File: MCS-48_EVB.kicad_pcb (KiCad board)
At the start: 2 copper layers, 36 parts, among them CON1 BARREL_JACK, P1 CONN_01X06, P10 CONN_01X08, P11 CONN_01X06, P2 CONN_01X06, P3 CONN_01X08, P4 CONN_01X08, P5 CONN_01X03, P6 CONN_01X03, P7 CONN_01X02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

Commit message: Working on component placement
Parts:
- C2, C4: moved to B.Cu
- moved U5 135.6 mm to (75.8, 97.2), turned to 180 degrees
- moved DS1 127.2 mm to (94.8, 52.9)
- moved U4 123.8 mm to (51.1, 97.2), turned to 180 degrees
- moved P3 109.5 mm to (52.1, 53.1), turned to 270 degrees
- moved U3 105.6 mm to (51.1, 139.8), turned to 180 degrees
- moved RV1 89.1 mm to (71.8, 59.8)
- moved P8 88.6 mm to (59.9, 104.3)
- moved U2 86.1 mm to (71.2, 139.8), turned to 180 degrees
- moved C2 78.7 mm to (69.9, 108.6), turned to 180 degrees
- moved C4 78.6 mm to (70.0, 103.7), turned to 180 degrees
- moved Y1 73.2 mm to (75.4, 108.6), turned to 90 degrees
- moved SW1 72.7 mm to (88.8, 146.5)
- moved P2 69.8 mm to (100.0, 155.2)
- moved CON1 68.8 mm to (196.2, 55.3), turned to 180 degrees
- moved C8 63.2 mm to (188.6, 56.2), turned to 90 degrees
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
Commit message: Finished component placement.
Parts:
- added C11: 100n, Capacitors_SMD:C_0805_HandSoldering, B.Cu at (38.9, 96.0)
- C1, C10, C3, C5, C6, C7, C9, R1, R2, R3: moved to B.Cu
- moved C5 101.7 mm to (67.4, 143.0), turned to 180 degrees
- moved C6 98.3 mm to (48.0, 138.4), turned to 90 degrees
- moved P3 96.1 mm to (59.0, 148.9)
- moved P6 94.9 mm to (77.0, 114.1), turned to 90 degrees
- moved C9 91.7 mm to (63.6, 95.9), turned to 90 degrees
- moved R3 84.9 mm to (61.3, 101.3), turned to 180 degrees
- moved P5 77.0 mm to (77.3, 149.0), turned to 90 degrees
- moved P2 65.9 mm to (153.0, 116.0), turned to 180 degrees
- moved C8 58.7 mm to (145.0, 95.5)
- moved P7 57.3 mm to (137.5, 145.2)
- moved CON1 57.2 mm to (154.6, 94.7)
- moved R1 54.4 mm to (90.6, 101.5)
- moved C1 51.6 mm to (98.5, 128.3), turned to 90 degrees
- moved C7 48.9 mm to (90.5, 99.2)
- moved R2 47.2 mm to (125.7, 147.7)
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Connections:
- U4 pad 28: VCC -> +5V

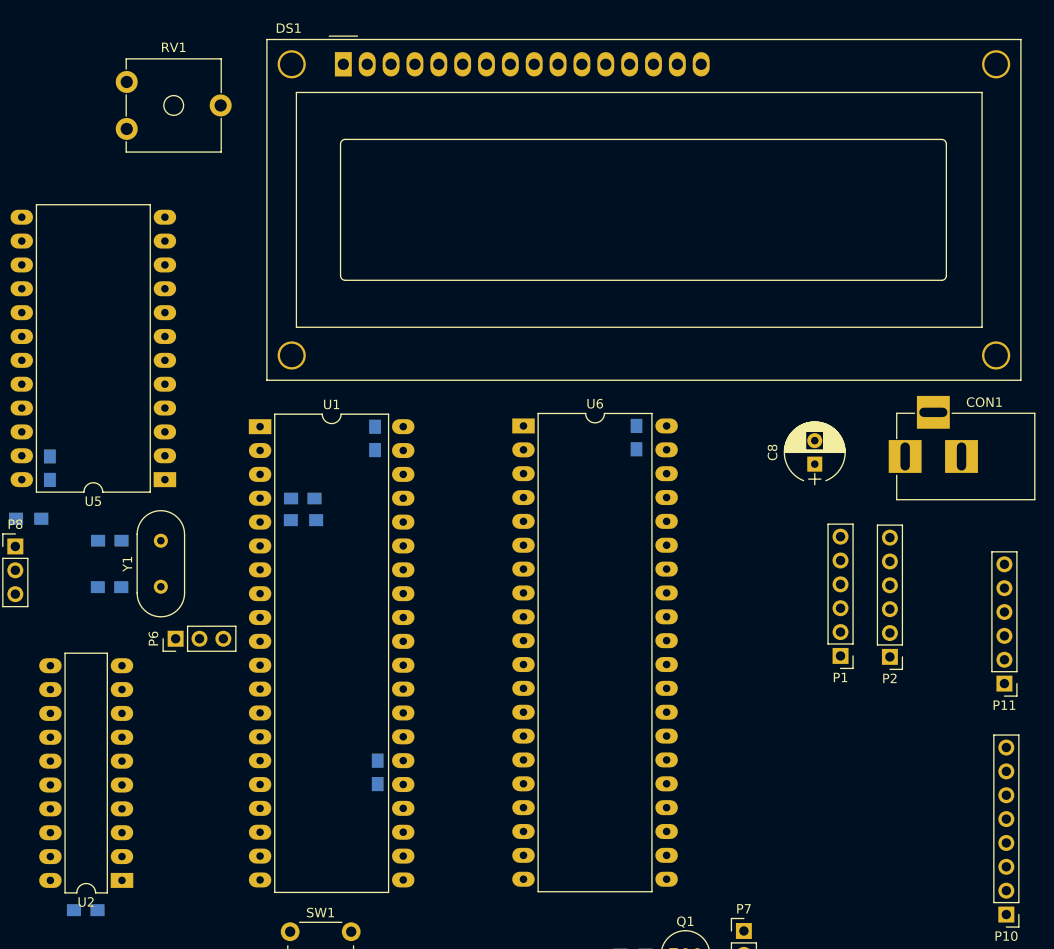
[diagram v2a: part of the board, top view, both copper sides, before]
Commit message: Added board outline.
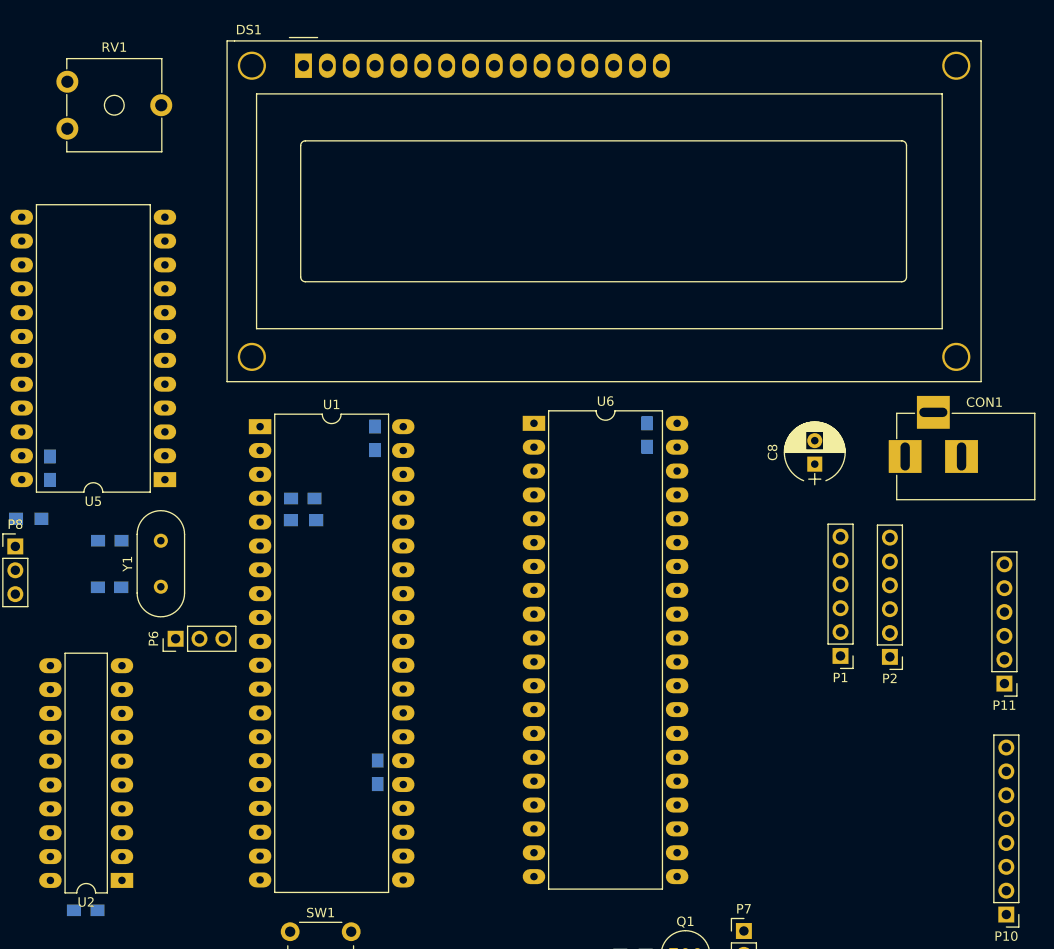
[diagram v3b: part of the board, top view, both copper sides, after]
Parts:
- moved RV1 6.32 mm to (65.4, 59.8)
- moved DS1 4.24 mm to (90.6, 53.1)
- moved C10 1.15 mm to (127.2, 92.4)
- moved U6 1.15 mm to (115.1, 91.2)
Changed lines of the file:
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@@
     (area 0 0 0 0)
     (thickness 1.6)
-    (drawings 0)
+    (drawings 6)
     (tracks 0)
     (zones 0)
@@
   )
   (module Capacitors_SMD:C_0805_HandSoldering (layer B.Cu)
-    (at 126.0348 92.6846 270)
+    (at 127.1524 92.4052 270)
     (descr "Capacitor SMD 0805, hand soldering")
     (tags "capacitor 0805")
@@
   )
   (module Display:WC1602A (layer F.Cu)
-    (at 94.8182 52.9336)
+    (at 90.5764 53.086)
     (descr "LCD 16x2 http://www.wincomlcd.com/pdf/WC1602A-SFYLYHTC06.pdf")
     (tags "LCD 16x2 Alphanumeric 16pin")
@@
   )
   (module Potentiometers:Potentiometer_Trimmer_ACP_CA9v_Horizontal_Px10.0mm_Py5.0mm (layer F.Cu)
-    (at 71.755 59.817)
+    (at 65.4304 59.7916)
     (descr "Potentiometer, horizontally mounted, Omeg PC16PU, Omeg PC16PU, Omeg PC16PU, Vishay/Spectrol 248GJ/249GJ Single, Vishay/Spectrol 248GJ/249GJ Single, Vishay/Spectrol 248GJ/249GJ Single, Vishay/Spectrol 248GH/249GH Single, Vishay/Spectrol 148/149 Single, Vishay/Spectrol 148/149 Single, Vishay/Spectrol 148/149 Single, Vishay/Spectrol 148A/149A Single with mounting plates, Vishay/Spectrol 148/149 Double, Vishay/Spectrol 148A/149A Double with mounting plates, Piher PC-16 Single, Piher PC-16 Single, Piher PC-16 Single, Piher PC-16SV Single, Piher PC-16 Double, Piher PC-16 Triple, Piher T16H Single, Piher T16L Single, Piher T16H Double, Alps RK163 Single, Alps RK163 Double, Alps RK097 Single, Alps RK097 Double, Bourns PTV09A-2 Single with mounting sleve Single, Bourns PTV09A-1 with mounting sleve Single, Bourns PRS11S Single, Alps RK09K Single with mounting sleve Single, Alps RK09K with mounting sleve Single, Alps RK09L Single, Alps RK09L Single, Alps RK09L Double, Alps RK09L Double, Alps RK09Y Single, Bourns 3339S Single, Bourns 3339S Single, Bourns 3339P Single, Bourns 3339H Single, Vishay T7YA Single, Suntan TSR-3386H Single, Suntan TSR-3386H Single, Suntan TSR-3386P Single, Vishay T73XX Single, Vishay T73XX Single, Vishay T73YP Single, Piher PT-6h Single, Piher PT-6v Single, Piher PT-6v Single, Piher PT-10h2.5 Single, Piher PT-10h5 Single, Piher PT-101h3.8 Single, Piher PT-10v10 Single, Piher PT-10v10 Single, Piher PT-10v5 Single, Piher PT-15h5 Single, Piher PT-15h2.5 Single, Piher PT-15B Single, Piher PT-15hc5 Single, Piher PT-15v12.5 Single, Piher PT-15v12.5 Single, Piher PT-15v15 Single, Piher PT-15v15 Single, ACP CA6h Single, ACP CA6v Single, ACP CA6v Single, ACP CA6VSMD Single, ACP CA6VSMD Single, ACP CA9h2.5 Single, ACP CA9h3.8 Single, ACP CA9h5 Single, ACP CA9V Single, http://www.acptechnologies.com/wp-content/uploads/2016/12/ACP-CAT%C3%81LOGO-ENTERO-2016.pdf")
     (tags "Potentiometer horizontal  Omeg PC16PU  Omeg PC16PU  Omeg PC16PU  Vishay/Spectrol 248GJ/249GJ Single  Vishay/Spectrol 248GJ/249GJ Single  Vishay/Spectrol 248GJ/249GJ Single  Vishay/Spectrol 248GH/249GH Single  Vishay/Spectrol 148/149 Single  Vishay/Spectrol 148/149 Single  Vishay/Spectrol 148/149 Single  Vishay/Spectrol 148A/149A Single with mounting plates  Vishay/Spectrol 148/149 Double  Vishay/Spectrol 148A/149A Double with mounting plates  Piher PC-16 Single  Piher PC-16 Single  Piher PC-16 Single  Piher PC-16SV Single  Piher PC-16 Double  Piher PC-16 Triple  Piher T16H Single  Piher T16L Single  Piher T16H Double  Alps RK163 Single  Alps RK163 Double  Alps RK097 Single  Alps RK097 Double  Bourns PTV09A-2 Single with mounting sleve Single  Bourns PTV09A-1 with mounting sleve Single  Bourns PRS11S Single  Alps RK09K Single with mounting sleve Single  Alps RK09K with mounting sleve Single  Alps RK09L Single  Alps RK09L Single  Alps RK09L Double  Alps RK09L Double  Alps RK09Y Single  Bourns 3339S Single  Bourns 3339S Single  Bourns 3339P Single  Bourns 3339H Single  Vishay T7YA Single  Suntan TSR-3386H Single  Suntan TSR-3386H Single  Suntan TSR-3386P Single  Vishay T73XX Single  Vishay T73XX Single  Vishay T73YP Single  Piher PT-6h Single  Piher PT-6v Single  Piher PT-6v Single  Piher PT-10h2.5 Single  Piher PT-10h5 Single  Piher PT-101h3.8 Single  Piher PT-10v10 Single  Piher PT-10v10 Single  Piher PT-10v5 Single  Piher PT-15h5 Single  Piher PT-15h2.5 Single  Piher PT-15B Single  Piher PT-15hc5 Single  Piher PT-15v12.5 Single  Piher PT-15v12.5 Single  Piher PT-15v15 Single  Piher PT-15v15 Single  ACP CA6h Single  ACP CA6v Single  ACP CA6v Single  ACP CA6VSMD Single  ACP CA6VSMD Single  ACP CA9h2.5 Single  ACP CA9h3.8 Single  ACP CA9h5 Single  ACP CA9V Single")
@@
   )
   (module Housings_DIP:DIP-40_W15.24mm_LongPads (layer F.Cu)
-    (at 113.9952 91.44)
+    (at 115.1128 91.1606)
     (descr "40-lead though-hole mounted DIP package, row spacing 15.24 mm (600 mils), LongPads")
     (tags "THT DIP DIL PDIP 2.54mm 15.24mm 600mil LongPads")
@@
     )
   )
+  (gr_line (start 31.7754 48.895) (end 31.9024 48.895) (angle 90) (layer Margin) (width 0.2))
+  (gr_line (start 31.7754 152.5524) (end 31.7754 48.895) (angle 90) (layer Margin) (width 0.2))
+  (gr_line (start 79.375 48.895) (end 31.8008 48.895) (angle 90) (layer Margin) (width 0.2))
+  (gr_line (start 167.4368 152.5524) (end 31.8008 152.5524) (angle 90) (layer Margin) (width 0.2))
+  (gr_line (start 167.4368 48.895) (end 167.4368 152.5524) (angle 90) (layer Margin) (width 0.2))
+  (gr_line (start 79.375 48.895) (end 167.4368 48.895) (angle 90) (layer Margin) (width 0.2))
 )

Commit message: Working on spaghetti-tracing
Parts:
- moved C5 29.6 mm to (69.4, 113.4), turned to 0 degrees
- moved U2 24.7 mm to (63.0, 116.6), turned to 0 degrees
- moved P1 5.37 mm to (153.1, 116.3)
- moved P2 4.00 mm to (149.0, 116.3)
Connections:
- U3 pad 28: VCC -> +5V
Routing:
- net +5V: track 0.00 -> 637.1 mm
- net /~RESET: track 0.00 -> 103.2 mm, vias 0 -> 1
- net /PC5: track 0.00 -> 101.9 mm
- net /PC4: track 0.00 -> 92.2 mm
- net /PC3: track 0.00 -> 91.0 mm, vias 0 -> 2
- net /LD0: track 0.00 -> 81.6 mm, vias 0 -> 1
- net /T1: track 0.00 -> 78.0 mm, vias 0 -> 1
- net /LD1: track 0.00 -> 77.5 mm, vias 0 -> 1
- net /LD2: track 0.00 -> 77.2 mm, vias 0 -> 1
- net /LD3: track 0.00 -> 77.1 mm, vias 0 -> 1
- net /P2.7: track 0.00 -> 73.9 mm
- net /LE: track 0.00 -> 67.8 mm, vias 0 -> 1
- net /LRS: track 0.00 -> 65.2 mm, vias 0 -> 1
- net /RESET: track 0.00 -> 64.5 mm
- net /DB7: track 0.00 -> 60.7 mm, vias 0 -> 1
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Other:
- net class Default: via_dia 0.6 -> 0.5; via_drill 0.4 -> 0.3
- net class HC_Power added: clearance 0.2, trace_width 1, via_dia 1, via_drill 0.5
- net class Power added: clearance 0.2, trace_width 0.5, via_dia 0.8, via_drill 0.5
- net class Signal added: clearance 0.2, trace_width 0.5, via_dia 0.6, via_drill 0.4

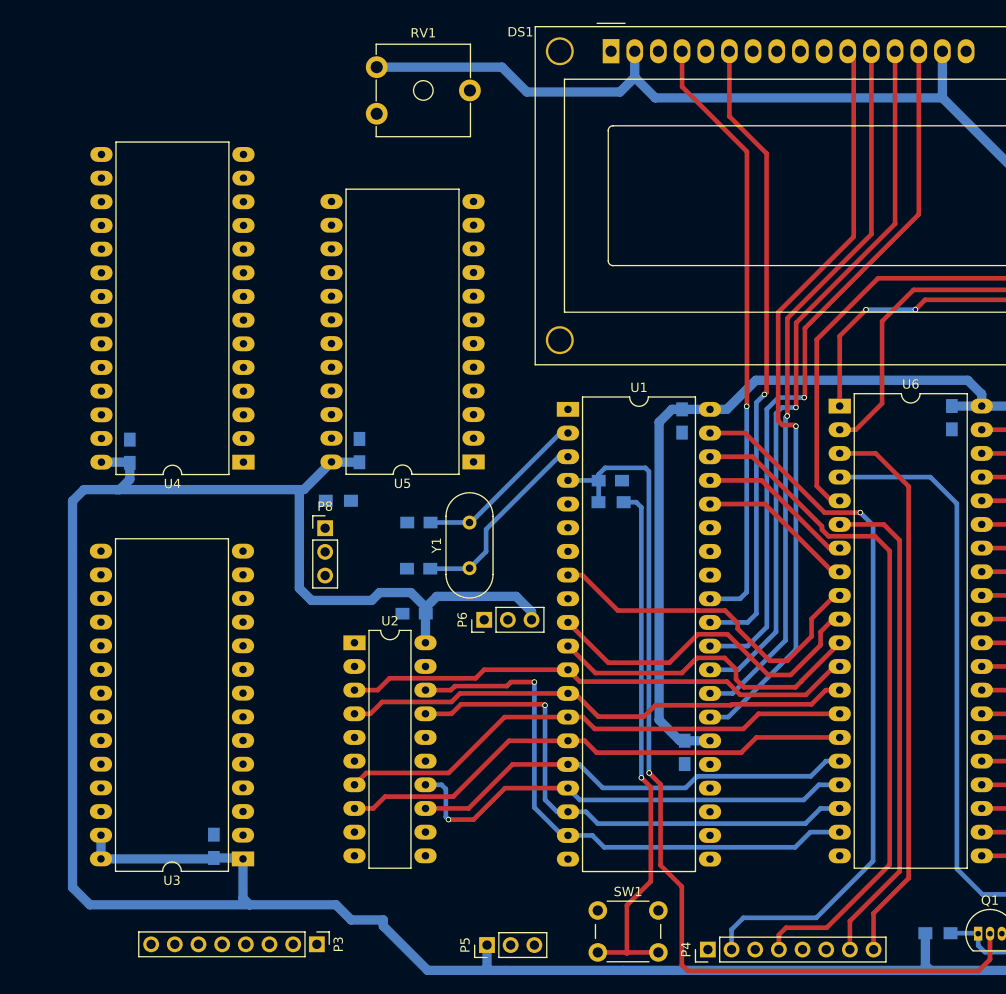
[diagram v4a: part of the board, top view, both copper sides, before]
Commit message: Working on spaghetti-tracing. Only GND left.
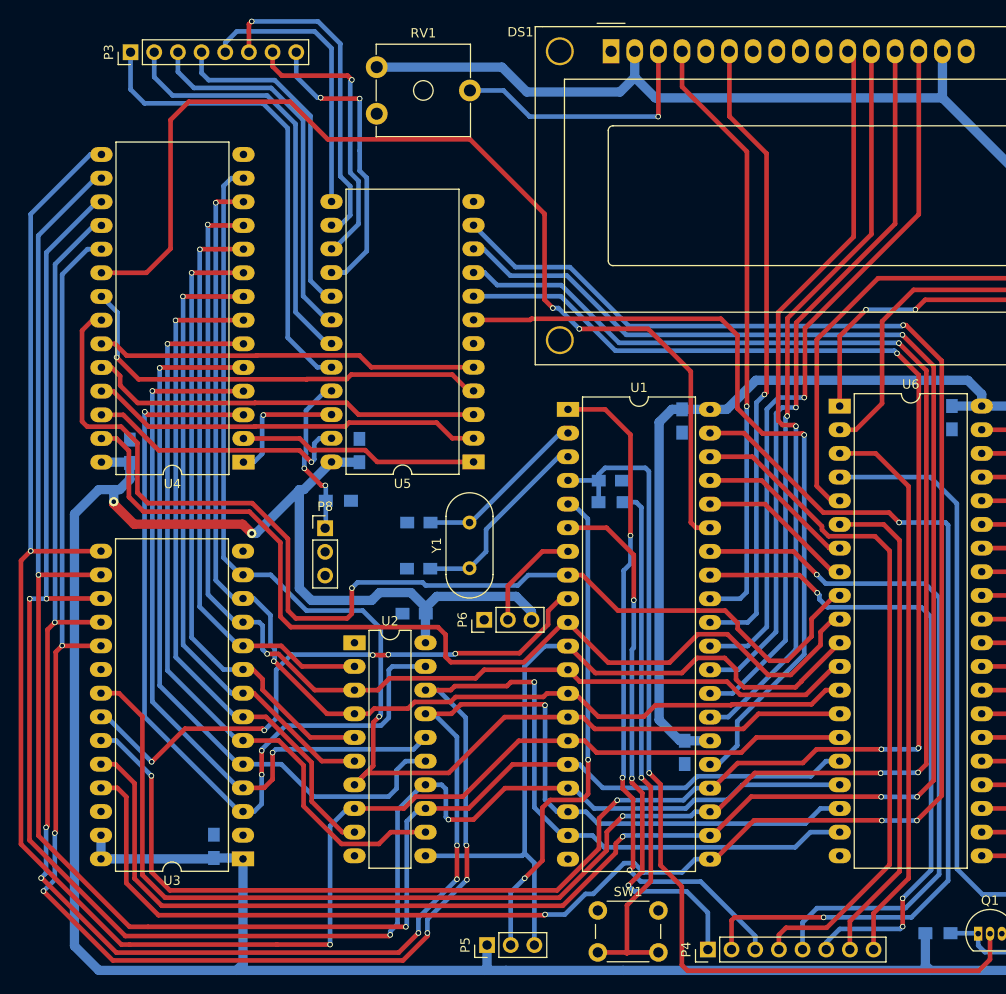
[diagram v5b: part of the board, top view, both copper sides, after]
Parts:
- moved P3 97.8 mm to (39.0, 53.2), turned to 90 degrees
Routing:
- net /A8: track 0.00 -> 210.5 mm, vias 0 -> 4
- net /A10: track 0.00 -> 209.9 mm, vias 0 -> 4
- net /A9: track 0.00 -> 206.8 mm, vias 0 -> 4
- net /A11: track 0.00 -> 200.3 mm, vias 0 -> 5
- net /DB7: track 60.7 -> 213.4 mm, vias 1 -> 7
- net /DB6: track 56.8 -> 206.8 mm, vias 1 -> 7
- net /DB5: track 50.4 -> 190.9 mm, vias 1 -> 4
- net /DB3: track 56.3 -> 195.9 mm, vias 0 -> 2
- net /DB4: track 48.6 -> 186.5 mm, vias 0 -> 2
- net /~RAM_S: track 0.00 -> 114.8 mm, vias 0 -> 2
- net /A7: track 0.00 -> 90.7 mm, vias 0 -> 3
- net /PROG: track 0.00 -> 85.4 mm, vias 0 -> 1
- net /~RD: track 37.3 -> 122.0 mm, vias 0 -> 1
- net /A4: track 0.00 -> 81.7 mm, vias 0 -> 1
- net /DB2: track 56.3 -> 136.6 mm, vias 0 -> 1
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
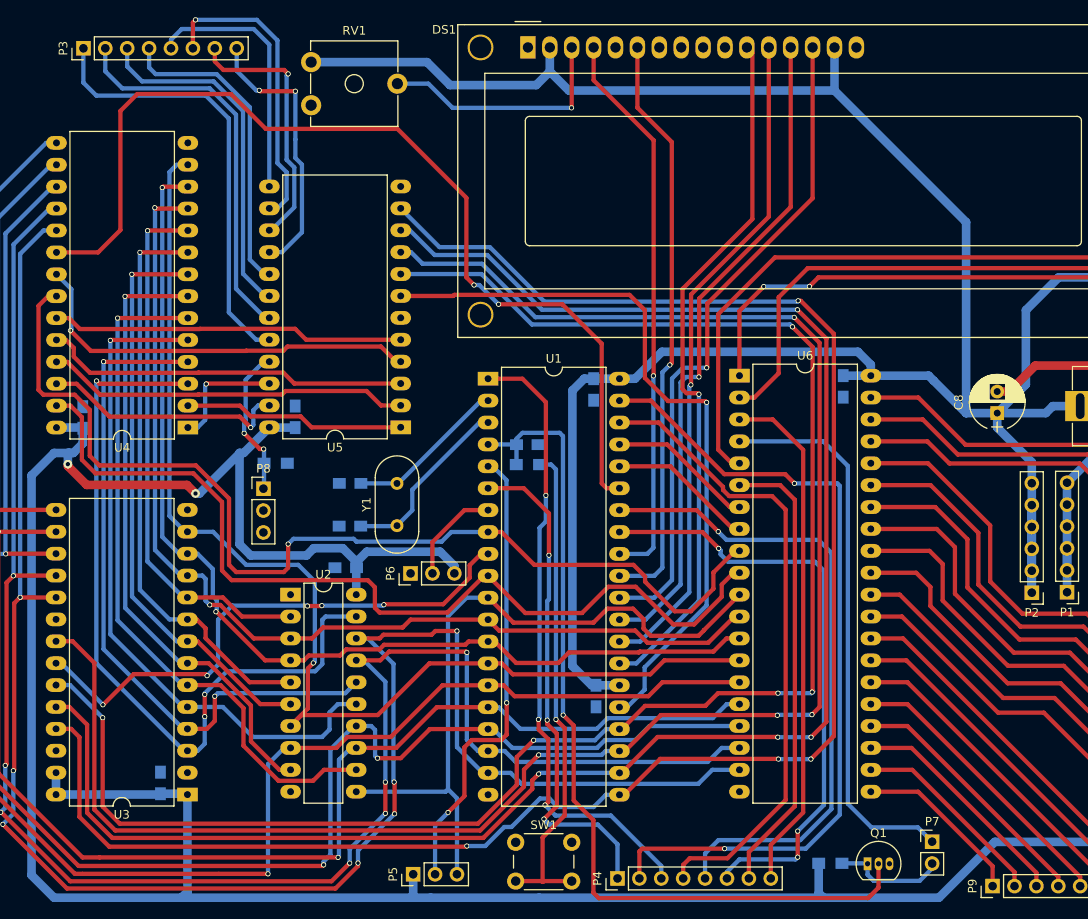
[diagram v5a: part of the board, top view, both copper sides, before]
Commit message: All nets connected
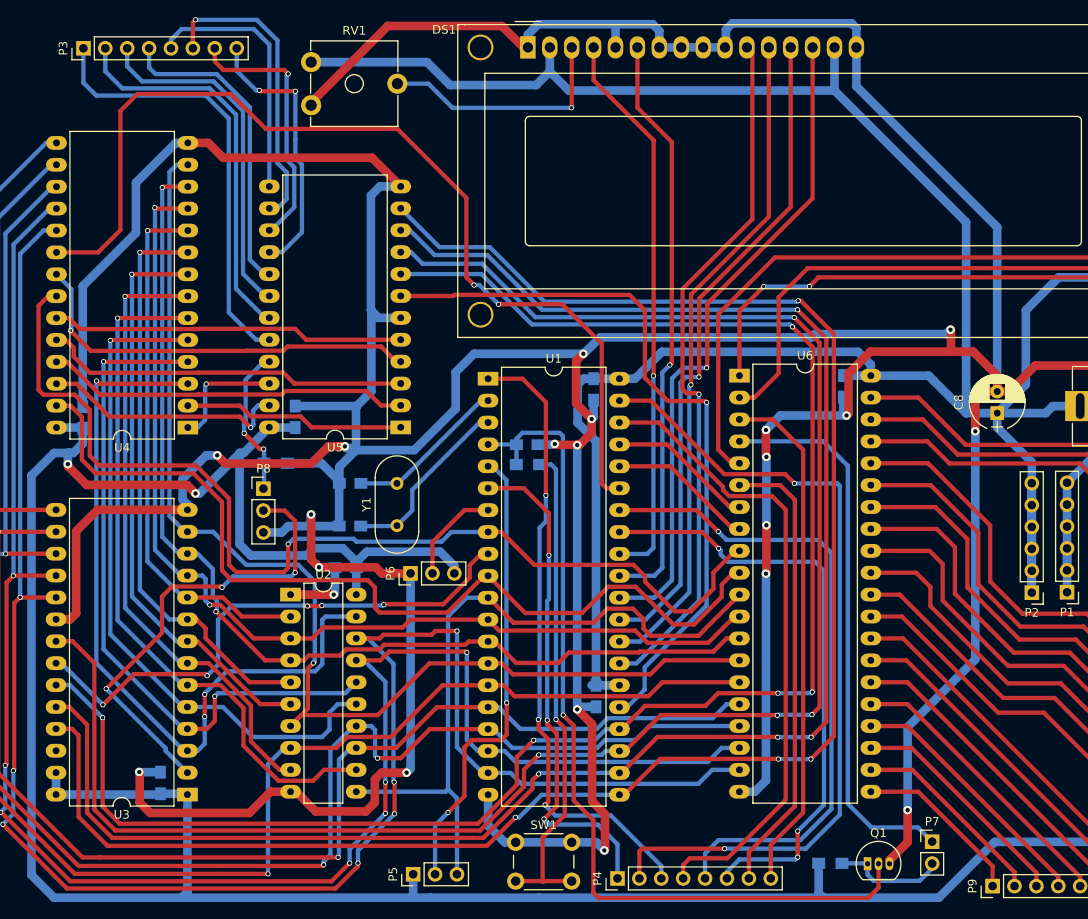
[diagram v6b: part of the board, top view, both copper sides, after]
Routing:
- net GND: track 47.6 -> 768.7 mm, vias 0 -> 21
- net /A12: track 0.00 -> 53.8 mm, vias 0 -> 3
- net +5V: track 651.4 -> 653.7 mm
- net /A8: track 210.5 -> 209.7 mm
